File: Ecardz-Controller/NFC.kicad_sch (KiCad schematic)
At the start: 0 parts

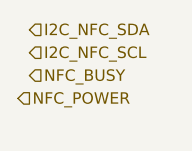
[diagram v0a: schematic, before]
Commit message: updated button pin choices, updated root
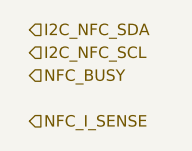
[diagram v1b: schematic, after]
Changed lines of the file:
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@@
 		)
 	)
-	(hierarchical_label "I2C_NFC_SDA"
+	(hierarchical_label "NFC_I_SENSE"
 		(shape input)
-		(at 50.8 38.1 0)
+		(at 50.8 48.26 0)
 		(fields_autoplaced yes)
 		(effects
@@
 		)
 	)
-	(hierarchical_label "NFC_POWER"
+	(hierarchical_label "I2C_NFC_SDA"
 		(shape input)
-		(at 49.53 45.72 0)
+		(at 50.8 38.1 0)
 		(fields_autoplaced yes)
 		(effects

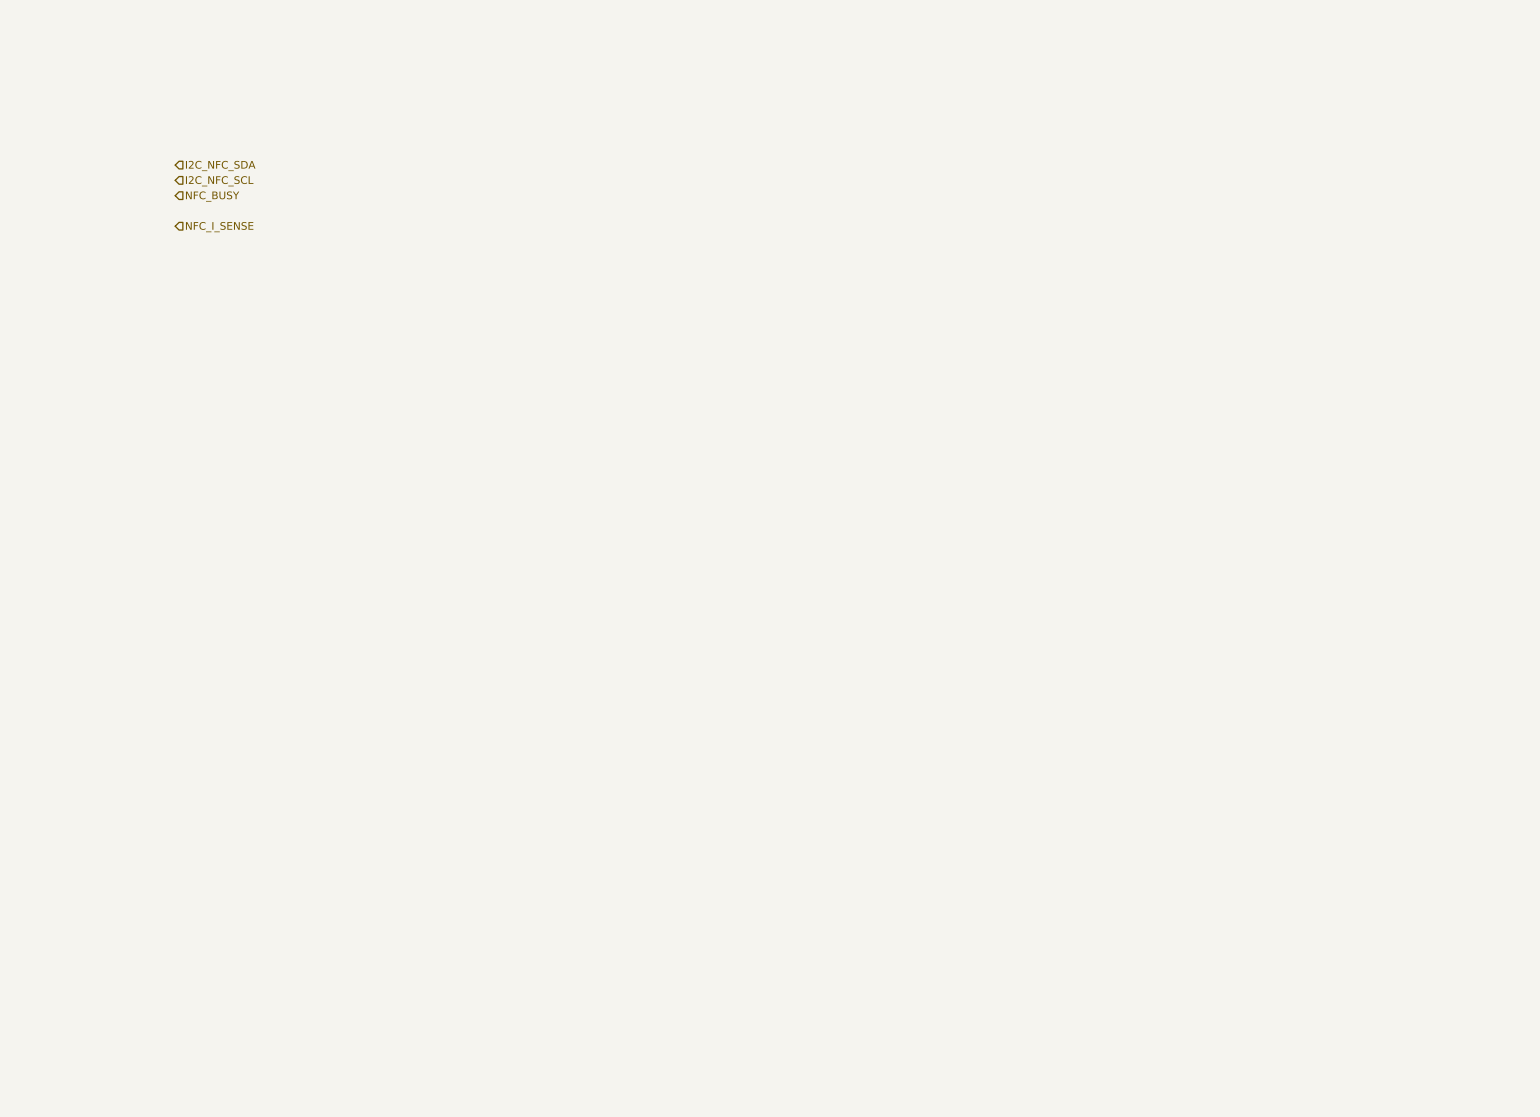
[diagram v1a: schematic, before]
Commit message: added NFC schematic
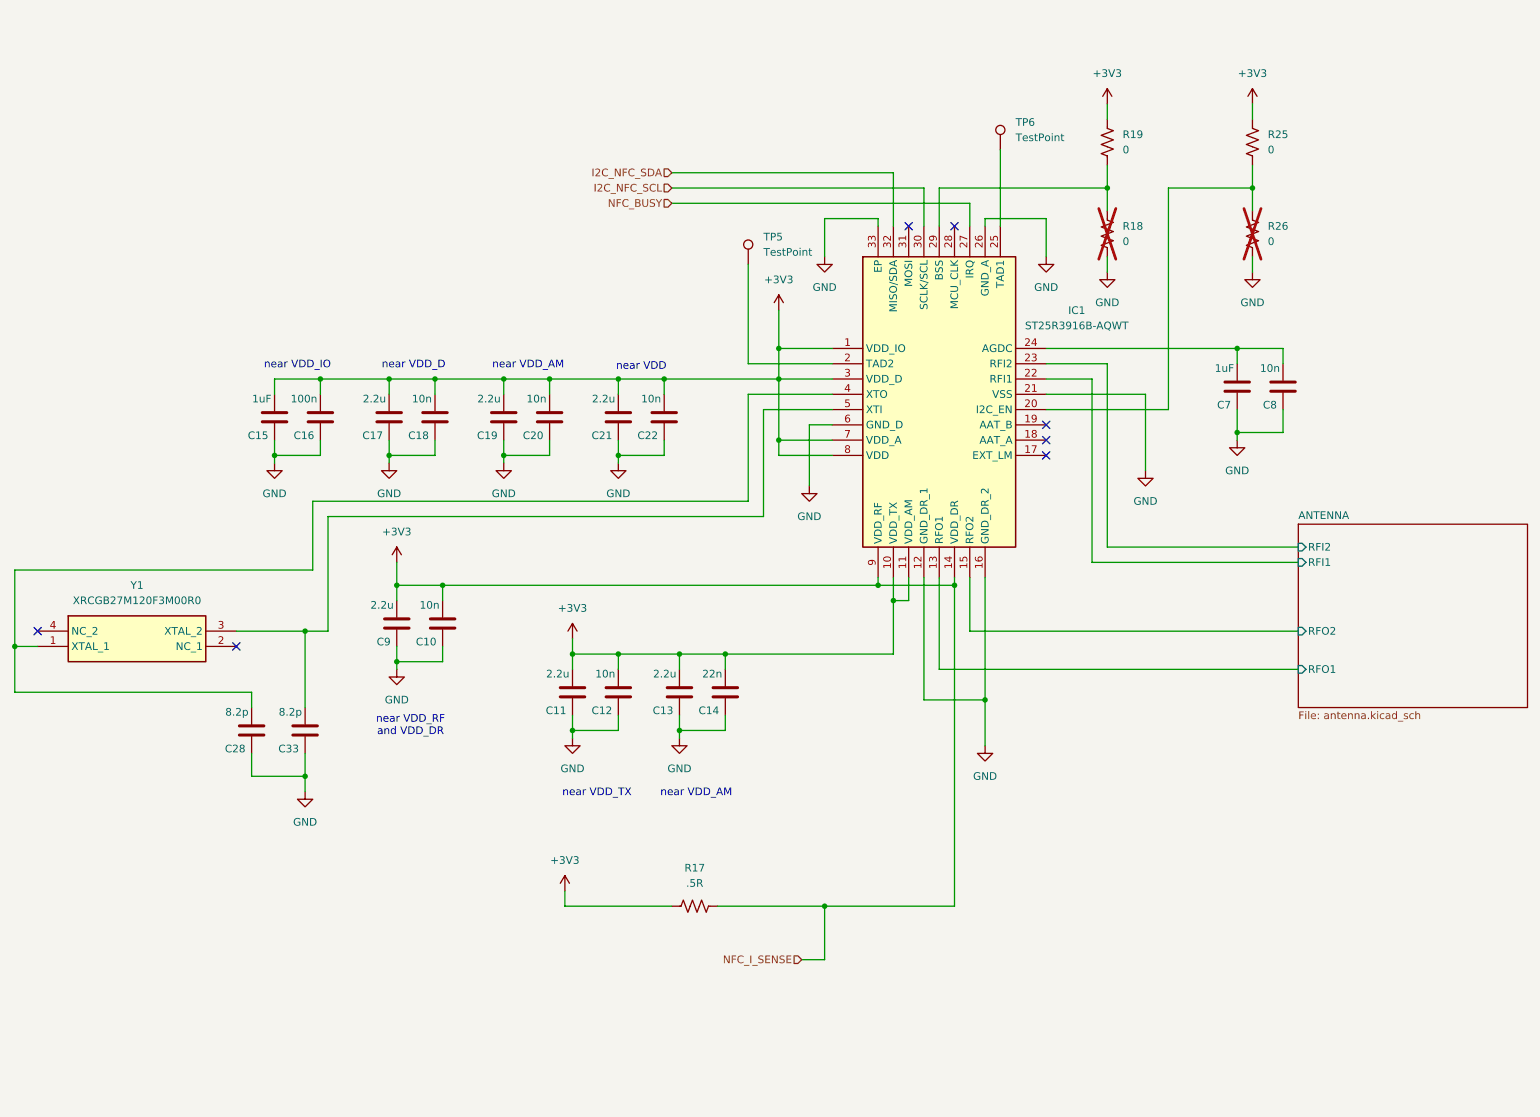
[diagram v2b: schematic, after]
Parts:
- added C10, C12, C18, C20, C22, C8: 10n, Capacitor_SMD:C_0603_1608Metric_Pad1.08x0.95mm_HandSolder, symbol Device:C
- added C11, C13, C17, C19, C21, C9: 2.2u, Capacitor_SMD:C_0603_1608Metric_Pad1.08x0.95mm_HandSolder, symbol Device:C
- added C14: 22n, Capacitor_SMD:C_0603_1608Metric_Pad1.08x0.95mm_HandSolder, symbol Device:C
- added C15, C7: 1uF, Capacitor_SMD:C_0603_1608Metric_Pad1.08x0.95mm_HandSolder, symbol Device:C
- added C16: 100n, Capacitor_SMD:C_0603_1608Metric_Pad1.08x0.95mm_HandSolder, symbol Device:C
- added C28, C33: 8.2p, Capacitor_SMD:C_0603_1608Metric_Pad1.08x0.95mm_HandSolder, symbol Device:C
- added IC1: ST25R3916B-AQWT, QFN50P500X500X100-33N-D, symbol SamacSys_Parts:ST25R3916B-AQWT
- added R17: .5R, Resistor_SMD:R_0603_1608Metric_Pad0.98x0.95mm_HandSolder, symbol Device:R_US
- added R18, R19, R25, R26: 0, Resistor_SMD:R_0603_1608Metric_Pad0.98x0.95mm_HandSolder, symbol Device:R_US
- added TP5, TP6: TestPoint, TestPoint:TestPoint_Pad_1.0x1.0mm, symbol Connector:TestPoint
- added Y1: XRCGB27M120F3M00R0, XRCGB, symbol SamacSys_Parts:XRCGB27M120F3M00R0
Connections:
- net I2C_NFC_SCL: now also IC1.30 (SCLK/SCL)
- net I2C_NFC_SDA: now also IC1.32 (MISO/SDA)
- net NFC_BUSY: now also IC1.27 (IRQ)
- new net: IC1.20 (I2C_EN), R25.1, R26.2
- new net: IC1.2 (TAD2), TP5.1
- new net: C7.2, C8.2, IC1.24 (AGDC)
- new net: IC1.25 (TAD1), TP6.1
- new net: IC1.29 (BSS), R18.2, R19.1
- new net: C28.2, IC1.4 (XTO), Y1.1 (XTAL_1)
- new net: C33.2, IC1.5 (XTI), Y1.3 (XTAL_2)
- new net +3V3: C10.2, C11.2, C12.2, C13.2, C14.2, C15.2, C16.2, C17.2, C18.2, C19.2, C20.2, C21.2, C22.2, C9.2, IC1.1 (VDD_IO), IC1.10 (VDD_TX), IC1.11 (VDD_AM), IC1.14 (VDD_DR), IC1.3 (VDD_D), IC1.7 (VDD_A), IC1.8 (VDD), IC1.9 (VDD_RF), R17.1, R17.2, R19.2, R25.2
- new net ANTENNA/RFI1: IC1.22 (RFI1)
- new net ANTENNA/RFI2: IC1.23 (RFI2)
- new net ANTENNA/RFO1: IC1.13 (RFO1)
- new net ANTENNA/RFO2: IC1.15 (RFO2)
- new net GND: C10.1, C11.1, C12.1, C13.1, C14.1, C15.1, C16.1, C17.1, C18.1, C19.1, C20.1, C21.1, C22.1, C28.1, C33.1, C7.1, C8.1, C9.1, IC1.12 (GND_DR_1), IC1.16 (GND_DR_2), IC1.21 (VSS), IC1.26 (GND_A), IC1.33 (EP), IC1.6 (GND_D), R18.1, R26.1
- no-connect marks 0 -> 7
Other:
- added sheet ANTENNA (antenna.kicad_sch)
- note added: "near VDD"
- note added: "near VDD_AM"
- note added: "near VDD_D"
- note added: "near VDD_IO"
- note added: "near VDD_RF and VDD_DR"
- note added: "near VDD_TX"

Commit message: initial work on controller layout
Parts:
- C1: renamed from C28; Part Number (none) -> GRM0335C1H8R2DA01D
- C3: renamed from C33; Part Number (none) -> GRM0335C1H8R2DA01D
- renumbered C20 to C10, C21 to C12, C12 to C13, C22 to C14, C13 to C15, C14 to C16, C7 to C17, C8 to C18, C15 to C2, C16 to C4, C17 to C5, C9 to C6, C18 to C7, C10 to C8, C19 to C9, R17 to R1, R19 to R2, R18 to R3, R25 to R4, R26 to R5, TP5 to TP1, TP6 to TP2
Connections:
- net +3V3: no longer C10.2, C15.2, C16.2, C5.2, C6.2, C7.2, C8.2, C9.2, IC1.11 (VDD_AM), IC1.14 (VDD_DR), IC1.3 (VDD_D), IC1.7 (VDD_A), IC1.9 (VDD_RF), R1.2
- new net: C5.2, C7.2, IC1.3 (VDD_D)
- new net: C10.2, C9.2, IC1.7 (VDD_A)
- new net: C15.2, C16.2, IC1.11 (VDD_AM)
- new net NFC_I_SENSE: C6.2, C8.2, IC1.14 (VDD_DR), IC1.9 (VDD_RF), R1.2
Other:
- note added: "near VDD_A"
- moved on the sheet: C10, C12, C14, C2, C4, C5, C7, C9

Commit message: did bulk of controller layout apart from the antenna, added some NCs and other minor clean ups on schematic
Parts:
- IC1: footprint QFN50P500X500X100-33N-D -> samacsys:QFN50P500X500X100-33N-D
- TP1, TP2: footprint TestPoint:TestPoint_Pad_1.0x1.0mm -> TestPoint:TestPoint_Pad_D3.0mm
- Y1: footprint XRCGB -> samacsys:XRCGB
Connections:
- net ANTENNA/AAT_A: now reaches IC1.18 (AAT_A)
- net ANTENNA/AAT_B: now reaches IC1.19 (AAT_B)
- no-connect marks 7 -> 5
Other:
- sheet ANTENNA ports: added AAT_A, AAT_B; removed none
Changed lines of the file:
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@@
 	)
 	(no_connect
-		(at 195.58 83.82)
-	)
-	(no_connect
 		(at 60.96 118.11)
 	)
 	(no_connect
-		(at 195.58 81.28)
-	)
-	(no_connect
 		(at 172.72 48.26)
 	)
@@
 	(wire
 		(pts
+			(xy 195.58 83.82) (xy 198.12 83.82)
+		)
+		(stroke
+			(width 0)
+			(type default)
+		)
+	)
+	(wire
+		(pts
 			(xy 134.62 132.08) (xy 142.24 132.08)
 		)
@@
 	(wire
 		(pts
+			(xy 200.66 81.28) (xy 195.58 81.28)
+		)
+		(stroke
+			(width 0)
+			(type default)
+		)
+	)
+	(wire
+		(pts
 			(xy 205.74 38.1) (xy 205.74 41.91)
 		)
@@
 	(wire
 		(pts
+			(xy 200.66 109.22) (xy 200.66 81.28)
+		)
+		(stroke
+			(width 0)
+			(type default)
+		)
+	)
+	(wire
+		(pts
 			(xy 158.75 81.28) (xy 158.75 91.44)
 		)
@@
 	(wire
 		(pts
+			(xy 198.12 83.82) (xy 198.12 111.76)
+		)
+		(stroke
+			(width 0)
+			(type default)
+		)
+	)
+	(wire
+		(pts
 			(xy 96.52 59.69) (xy 96.52 83.82)
 		)
@@
 	(wire
 		(pts
+			(xy 198.12 111.76) (xy 237.49 111.76)
+		)
+		(stroke
+			(width 0)
+			(type default)
+		)
+	)
+	(wire
+		(pts
 			(xy 205.74 71.12) (xy 205.74 101.6)
 		)
@@
 	(wire
 		(pts
+			(xy 237.49 109.22) (xy 200.66 109.22)
+		)
+		(stroke
+			(width 0)
+			(type default)
+		)
+	)
+	(wire
+		(pts
 			(xy 187.96 35.56) (xy 187.96 48.26)
 		)
@@
 			)
 		)
-		(property "Footprint" "QFN50P500X500X100-33N-D"
+		(property "Footprint" "samacsys:QFN50P500X500X100-33N-D"
 			(at 191.77 150.8 0)
 			(effects
@@
 			)
 		)
-		(property "Footprint" "TestPoint:TestPoint_Pad_1.0x1.0mm"
+		(property "Footprint" "TestPoint:TestPoint_Pad_D3.0mm"
 			(at 151.13 54.61 0)
 			(effects
@@
 			)
 		)
-		(property "Footprint" "XRCGB"
+		(property "Footprint" "samacsys:XRCGB"
 			(at 57.15 210.49 0)
 			(effects
@@
 			)
 		)
-		(property "Footprint" "TestPoint:TestPoint_Pad_1.0x1.0mm"
+		(property "Footprint" "TestPoint:TestPoint_Pad_D3.0mm"
 			(at 193.04 35.56 0)
 			(effects
@@
 			(effects
 				(font
+					(size 1.27 1.27)
+				)
+				(justify left)
+			)
+		)
+		(pin "AAT_A" input
+			(at 237.49 111.76 180)
+			(effects
+				(font
+					(size 1.27 1.27)
+				)
+				(justify left)
+			)
+		)
+		(pin "AAT_B" input
+			(at 237.49 109.22 180)
+			(effects
+				(font

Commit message: controller updates
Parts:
- added R1: 0, Resistor_SMD:R_0603_1608Metric_Pad0.98x0.95mm_HandSolder, symbol Device:R_US
- added TP10: TestPoint, TestPoint:TestPoint_Pad_D3.0mm, symbol Connector:TestPoint
- C10: renamed from C4; Part Number (none) -> CC0603KRX7R7BB104
- C11, C15, C6: Part Number (none) -> CL10A225KO8NNNC
- C12: renamed from C13; Part Number (none) -> CC0603KRX7R9BB103
- C13: renamed from C12; Part Number (none) -> CL10A225KO8NNNC
- C14, C18, C8: Part Number (none) -> CC0603KRX7R9BB103
- C16: Part Number (none) -> GCM188R72A223KA37J
- C17: Part Number (none) -> CL10B105KP8NNNC
- C2: renamed from C5; Part Number (none) -> CL10A225KO8NNNC
- C3: renamed from C7; Part Number (none) -> CC0603KRX7R9BB103
- C5: renamed from C9; Part Number (none) -> CL10A225KO8NNNC
- C7: renamed from C10; Part Number (none) -> CC0603KRX7R9BB103
- C9: renamed from C2; Part Number (none) -> CL10B105KP8NNNC
- IC1: Part Number (none) -> ST25R3916B-AQWT
- R2: renamed from R1; Part Number (none) -> CSR0603FKR500
- R3: renamed from R2; Part Number (none) -> RMCF0603ZT0R00
- R4: renamed from R3; Part Number (none) -> RMCF0603ZT0R00
- R5: renamed from R4; Part Number (none) -> RMCF0603ZT0R00
- R6: renamed from R5; Part Number (none) -> RMCF0603ZT0R00
- Y1: Part Number (none) -> XRCGB27M120F3M00R0
- renumbered C3 to C4
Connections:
- net +3V3 renamed VDD_NFC
- net VDD_NFC: now also R1.1, TP10.1
- new net PWR: R1.2

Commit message: updates based on review
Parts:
- added R51: 0, Resistor_SMD:R_0603_1608Metric_Pad0.98x0.95mm_HandSolder, symbol Device:R_US
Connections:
- net VDD_NFC: now also R51.2
- net NFC_I_SENSE renamed NFC_I_SENSE_P
- new net NFC_I_SENSE_N: R51.1
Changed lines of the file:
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@@
 	)
 	(junction
+		(at 115.57 161.29)
+		(diameter 0)
+		(color 0 0 0 0)
+	)
+	(junction
 		(at 116.84 132.08)
 		(diameter 0)
@@
 	)
 	(junction
+		(at 146.05 161.29)
+		(diameter 0)
+		(color 0 0 0 0)
+	)
+	(junction
 		(at 180.34 107.95)
 		(diameter 0)
@@
 	)
 	(junction
-		(at 158.75 161.29)
-		(diameter 0)
-		(color 0 0 0 0)
-	)
-	(junction
 		(at 83.82 72.39)
 		(diameter 0)
@@
 	(wire
 		(pts
+			(xy 115.57 161.29) (xy 115.57 163.83)
+		)
+		(stroke
+			(width 0)
+			(type default)
+		)
+	)
+	(wire
+		(pts
 			(xy 134.62 132.08) (xy 134.62 133.35)
 		)
@@
 	(wire
 		(pts
-			(xy 154.94 170.18) (xy 158.75 170.18)
+			(xy 149.86 176.53) (xy 146.05 176.53)
 		)
 		(stroke
@@
 	(wire
 		(pts
+			(xy 120.65 176.53) (xy 115.57 176.53)
+		)
+		(stroke
+			(width 0)
+			(type default)
+		)
+	)
+	(wire
+		(pts
 			(xy 198.12 83.82) (xy 198.12 111.76)
 		)
@@
 	(wire
 		(pts
-			(xy 140.97 161.29) (xy 158.75 161.29)
+			(xy 140.97 161.29) (xy 146.05 161.29)
 		)
 		(stroke
@@
 	(wire
 		(pts
+			(xy 115.57 171.45) (xy 115.57 176.53)
+		)
+		(stroke
+			(width 0)
+			(type default)
+		)
+	)
+	(wire
+		(pts
 			(xy 170.18 106.68) (xy 170.18 116.84)
 		)
@@
 	(wire
 		(pts
-			(xy 158.75 161.29) (xy 180.34 161.29)
-		)
-		(stroke
-			(width 0)
-			(type default)
-		)
-	)
-	(wire
-		(pts
 			(xy 205.74 27.94) (xy 205.74 30.48)
 		)
@@
 	(wire
 		(pts
-			(xy 158.75 170.18) (xy 158.75 161.29)
+			(xy 146.05 176.53) (xy 146.05 161.29)
 		)
 		(stroke
@@
 		)
 	)
+	(wire
+		(pts
+			(xy 146.05 161.29) (xy 180.34 161.29)
+		)
+		(stroke
+			(width 0)
+			(type default)
+		)
+	)
 	(text "near VDD_RF\nand VDD_DR"
 		(exclude_from_sim no)
@@
 		)
 	)
-	(hierarchical_label "NFC_I_SENSE"
-		(shape input)
-		(at 154.94 170.18 180)
+	(hierarchical_label "NFC_I_SENSE_P"
+		(shape output)
+		(at 149.86 176.53 0)
 		(fields_autoplaced yes)
 		(effects
@@
 				(size 1.27 1.27)
 			)
-			(justify right)
+			(justify left)
 		)
 	)
@@
 		)
 	)
+	(hierarchical_label "NFC_I_SENSE_N"
+		(shape output)
+		(at 120.65 176.53 0)
+		(fields_autoplaced yes)
+		(effects
+			(font
+				(size 1.27 1.27)
+			)
+			(justify left)
+		)
+	)
 	(hierarchical_label "PWR"
 		(shape input)
@@
 					(unit 1)
 				)
+			)
+		)
+	)
+	(symbol
+		(lib_id "Device:R_US")
+		(at 115.57 167.64 180)
+		(unit 1)
+		(exclude_from_sim no)
+		(in_bom yes)
+		(on_board yes)
+		(dnp no)
+		(fields_autoplaced yes)
+		(property "Reference" "R51"
+			(at 118.11 166.3699 0)
+			(effects
+				(font
+					(size 1.27 1.27)
+				)
+				(justify right)
+			)
+		)
+		(property "Value" "0"
+			(at 118.11 168.9099 0)
+			(effects
+				(font
+					(size 1.27 1.27)
+				)
+				(justify right)
+			)
+		)
+		(property "Footprint" "Resistor_SMD:R_0603_1608Metric_Pad0.98x0.95mm_HandSolder"
+			(at 114.554 167.386 90)
+			(effects
+				(font
+					(size 1.27 1.27)
+				)
+				(hide yes)
+			)
+		)
+		(property "Datasheet" ""
+			(at 115.57 167.64 0)
+			(effects
+				(font
+					(size 1.27 1.27)
+				)
+				(hide yes)
+			)
+		)
+		(property "Description" "Resistor, US symbol"
+			(at 115.57 167.64 0)
+			(effects
+				(font
+					(size 1.27 1.27)
+				)
+				(hide yes)
+			)
+		)
+		(property "MANUFACTURER PART NUMBER" "CRCW0603590RFKEA"
+			(at 115.57 167.64 0)
+			(effects
+				(font
+					(size 1.27 1.27)
+				)
+				(hide yes)
+			)
+		)
+		(property "Digikey Part Number" "541-590HTR-ND"
+			(at 115.57 167.64 0)
+			(effects
+				(font
+					(size 1.27 1.27)
+				)
+				(hide yes)
+			)
+		)
+		(property "Part Number" "RMCF0603ZT0R00"
+			(at 115.57 167.64 0)
+			(effects
+				(font
+					(size 1.27 1.27)
+				)
+				(hide yes)
+			)
+		)
+		(pin "1"
+		)
+		(pin "2"
+		)
+		(instances
+			(project "Ecardz-Controller"
+				(path "/74270717-a116-451e-ac88-5a07ab66056e/414d1147-8205-4839-9169-5f8f29a4e15a"
+					(reference "R51")
+					(unit 1)
+				)

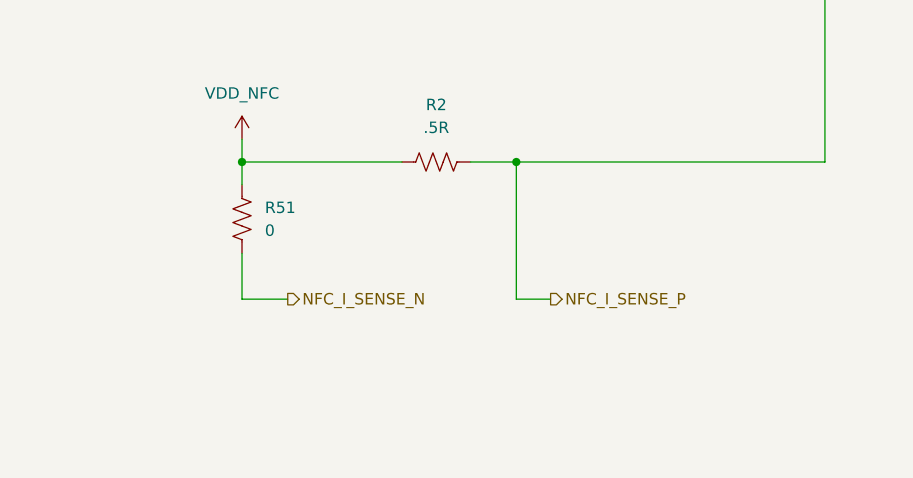
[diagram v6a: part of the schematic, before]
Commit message: added current sense resistor and modified buzzer circuit
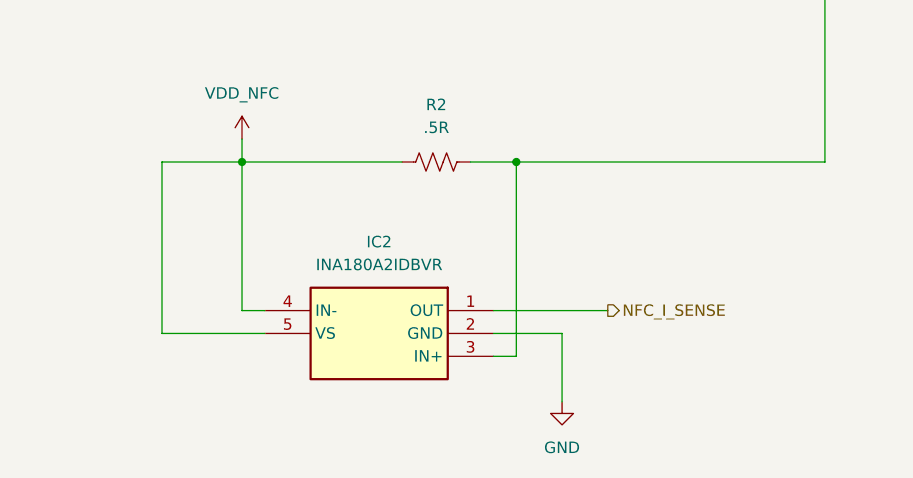
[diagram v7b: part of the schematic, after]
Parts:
- removed R51: 0, Resistor_SMD:R_0603_1608Metric_Pad0.98x0.95mm_HandSolder, symbol Device:R_US
- added IC2: INA180A2IDBVR, SOT95P280X145-5N, symbol SamacSys_Parts:INA180A2IDBVR
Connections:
- net GND: now also IC2.2 (GND)
- net VDD_NFC: now also IC2.4 (IN-), IC2.5 (VS)
- net NFC_I_SENSE_P: no longer names the net of C6.2, C8.2, IC1.14 (VDD_DR), IC1.9 (VDD_RF), R2.2
- net NFC_I_SENSE_P: now also IC2.3 (IN+)
- new net NFC_I_SENSE: IC2.1 (OUT)
